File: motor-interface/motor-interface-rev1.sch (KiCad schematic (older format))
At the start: 24 parts

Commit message: Done with 1st pass of interface board schematic
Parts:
- added RV? (x3): POT, symbol POT
- added U? (x2): SN74LV1T34, symbol SN74LV1T34
- R?: value R_Small -> 330R
- R?: value R_Small -> 500R
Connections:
- net +3V3: now also P?.2 (P2), U?.5 (VCC), U?.5 (VCC), U?.5 (VCC)
- net GND: now also RV?.3, RV?.3, RV?.3, U?.3 (GND), U?.3 (GND)
- net at P?.1 (P1), P?.13 (P13): now also U?.2 (A)
- net at P?.7 (P7), Q?.1 (G): now also U?.4 (Y); no longer P?.11 (P11)
- net +5V: now reaches D?.2 (A), P?.18 (P18), U?.1 (VI)
- net +5V: now also U?.5 (VCC), U?.5 (VCC), U?.5 (VCC)
- net at P?.19 (P19): now also RV?.1
- net at P?.21 (P21): now also RV?.1
- net at P?.23 (P23): now also RV?.1
- net at P?.14 (P14), P?.3 (P3): now also U?.4 (Y)
- net at P?.12 (P12), P?.5 (P5): now also U?.2 (A)
- net at P?.5 (P5), Q?.1 (G): now also U?.4 (Y); no longer P?.9 (P9)
- net at P?.14 (P14), R?.2: now also RV?.2
- net at P?.16 (P16), R?.2: now also RV?.2
- net at P?.18 (P18): now also RV?.2
- net at P?.6 (P6): now also U?.2 (A)
- new net: P?.11 (P11), U?.2 (A)
- new net: P?.9 (P9), U?.2 (A)
- no-connect marks 18 -> 17
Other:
- note added: "GND\nSCS - drv\nCS - temp\nX\nX\nSDI\nSDO\nEN-GATE\nDC-CAL\nX"
- note added: "Hall Effect Output Trim"
- note added: "nFAULT"
- note added: "nOCTW"
- note removed: "GND\nSCS\nX\nX\nX\nSDI\nSDO\nEN-GATE\nDC-CAL\nX"
- moved on the sheet: P?

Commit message: Performed annotation, added 2 missing gnds
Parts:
- gave numbers to parts that had none: 29
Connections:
- net GND: now also P2.4 (P4), P3.2 (P2)

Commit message: Added 3.3V conn to launch, added pots&volt.sensing
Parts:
- added P?: CONN_01X03, symbol CONN_01X03
- added P?: CONN_01X04, symbol CONN_01X04
- added RV? (x4): POT, symbol POT
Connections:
- net +3V3: now also P2.1 (P1)
- net GND: now also RV?.3, RV?.3, RV?.3, RV?.3
- net at P2.10 (P10): now also RV?.2
- net at P2.12 (P12): now also RV?.2
- net at P2.14 (P14), R3.2, RV1.2: now also P?.3 (P3)
- net at P2.16 (P16), R4.2, RV2.2: now also P?.2 (P2)
- net at P2.18 (P18), RV3.2: now also P?.1 (P1)
- net at P2.6 (P6): now also RV?.2
- net at P2.8 (P8): now also RV?.2
- new net: P?.1 (P1), RV?.1
- new net: P?.2 (P2), RV?.1
- new net: P?.3 (P3), RV?.1
- new net: P?.4 (P4), RV?.1
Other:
- note added: "+3.3V Regulator"
- note added: "+5V Buck"
- note added: "Hall Effect Debug"
- note added: "Launchpad Left"
- note added: "Launchpad Right"
- note added: "Motor Control Board"
- note added: "VC-FB\nVB-FB\nVA-FB\nDC-V-FB"
- note added: "Voltage Feedback Trim"
- note added: "Voltage Sensing"
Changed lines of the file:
@@
 Wire Wire Line
 	4900 4250 4800 4250
+$Comp
+L +3.3V #PWR?
+U 1 1 56FC658F
+P 2700 4100
+F 0 "#PWR?" H 2700 3950 50  0001 C CNN
+F 1 "+3.3V" H 2700 4240 50  0000 C CNN
+F 2 "" H 2700 4100 50  0000 C CNN
+F 3 "" H 2700 4100 50  0000 C CNN
+	1    2700 4100
+	1    0    0    -1
+$EndComp
+Wire Wire Line
+	2700 4100 2700 4250
+$Comp
+L CONN_01X03 P?
+U 1 1 56FC81E5
+P 3100 7700
+F 0 "P?" H 3100 7900 50  0000 C CNN
+F 1 "CONN_01X03" V 3200 7700 50  0000 C CNN
+F 2 "" H 3100 7700 50  0000 C CNN
+F 3 "" H 3100 7700 50  0000 C CNN
+	1    3100 7700
+	0    1    1    0
+$EndComp
+Text Notes 2750 7950 0    60   ~ 0
+Hall Effect Debug
+Wire Notes Line
+	2850 7850 3350 7850
+Wire Notes Line
+	3350 7850 3350 7450
+Wire Notes Line
+	3350 7450 2850 7450
+Wire Notes Line
+	2850 7450 2850 7850
+Wire Wire Line
+	3000 7500 3000 7300
+Connection ~ 3000 7300
+Wire Wire Line
+	3100 7500 3100 7250
+Connection ~ 3100 7250
+Wire Wire Line
+	3200 7500 3200 6750
+Connection ~ 3200 6750
+$Comp
+L CONN_01X04 P?
+U 1 1 56FC95E7
+P 5350 7100
+F 0 "P?" H 5350 7350 50  0000 C CNN
+F 1 "CONN_01X04" V 5450 7100 50  0000 C CNN
+F 2 "" H 5350 7100 50  0000 C CNN
+F 3 "" H 5350 7100 50  0000 C CNN
+	1    5350 7100
+	1    0    0    -1
+$EndComp
+Wire Wire Line
+	3850 6650 3850 4450
+Wire Wire Line
+	3850 4450 3200 4450
+Wire Wire Line
+	3800 6750 3800 4550
+Wire Wire Line
+	3800 4550 3200 4550
+Wire Wire Line
+	3750 6850 3750 4650
+Wire Wire Line
+	3750 4650 3200 4650
+Wire Wire Line
+	3700 4750 3700 7550
+Wire Wire Line
+	3700 4750 3200 4750
+Wire Notes Line
+	5150 6800 5150 7400
+Wire Notes Line
+	5150 7400 5550 7400
+Wire Notes Line
+	5550 7400 5550 6800
+Wire Notes Line
+	5550 6800 5150 6800
+Text Notes 5050 6750 0    60   ~ 0
+Voltage Sensing
+$Comp
+L POT RV?
+U 1 1 56FC9C0F
+P 4700 7550
+F 0 "RV?" H 4700 7450 50  0000 C CNN
+F 1 "POT" H 4700 7550 50  0000 C CNN
+F 2 "" H 4700 7550 50  0000 C CNN
+F 3 "" H 4700 7550 50  0000 C CNN
+	1    4700 7550
+	0    -1   1    0
+$EndComp
+$Comp
+L POT RV?
+U 1 1 56FC9CC4
+P 5050 7550
+F 0 "RV?" H 5050 7450 50  0000 C CNN
+F 1 "POT" H 5050 7550 50  0000 C CNN
+F 2 "" H 5050 7550 50  0000 C CNN
+F 3 "" H 5050 7550 50  0000 C CNN
+	1    5050 7550
+	0    -1   1    0
+$EndComp
+$Comp
+L POT RV?
+U 1 1 56FC9D25
+P 4000 7550
+F 0 "RV?" H 4000 7450 50  0000 C CNN
+F 1 "POT" H 4000 7550 50  0000 C CNN
+F 2 "" H 4000 7550 50  0000 C CNN
+F 3 "" H 4000 7550 50  0000 C CNN
+	1    4000 7550
+	0    -1   1    0
+$EndComp
+$Comp
+L POT RV?
+U 1 1 56FC9D8A
+P 4350 7550
+F 0 "RV?" H 4350 7450 50  0000 C CNN
+F 1 "POT" H 4350 7550 50  0000 C CNN
+F 2 "" H 4350 7550 50  0000 C CNN
+F 3 "" H 4350 7550 50  0000 C CNN
+	1    4350 7550
+	0    -1   1    0
+$EndComp
+$Comp
+L GND #PWR?
+U 1 1 56FCA3E0
+P 4000 7850
+F 0 "#PWR?" H 4000 7600 50  0001 C CNN
+F 1 "GND" H 4000 7700 50  0000 C CNN
+F 2 "" H 4000 7850 50  0000 C CNN
+F 3 "" H 4000 7850 50  0000 C CNN
+	1    4000 7850
+	1    0    0    -1
+$EndComp
+$Comp
+L GND #PWR?
+U 1 1 56FCA45B
+P 4350 7850
+F 0 "#PWR?" H 4350 7600 50  0001 C CNN
+F 1 "GND" H 4350 7700 50  0000 C CNN
+F 2 "" H 4350 7850 50  0000 C CNN
+F 3 "" H 4350 7850 50  0000 C CNN
+	1    4350 7850
+	1    0    0    -1
+$EndComp
+$Comp
+L GND #PWR?
+U 1 1 56FCA4CF
+P 4700 7850
+F 0 "#PWR?" H 4700 7600 50  0001 C CNN
+F 1 "GND" H 4700 7700 50  0000 C CNN
+F 2 "" H 4700 7850 50  0000 C CNN
+F 3 "" H 4700 7850 50  0000 C CNN
+	1    4700 7850
+	1    0    0    -1
+$EndComp
+$Comp
+L GND #PWR?
+U 1 1 56FCA543
+P 5050 7850
+F 0 "#PWR?" H 5050 7600 50  0001 C CNN
+F 1 "GND" H 5050 7700 50  0000 C CNN
+F 2 "" H 5050 7850 50  0000 C CNN
+F 3 "" H 5050 7850 50  0000 C CNN
+	1    5050 7850
+	1    0    0    -1
+$EndComp
+Wire Wire Line
+	4000 7800 4000 7850
+Wire Wire Line
+	4350 7800 4350 7850
+Wire Wire Line
+	4700 7800 4700 7850
+Wire Wire Line
+	5050 7800 5050 7850
+Wire Wire Line
+	5050 7300 5050 7250
+Wire Wire Line
+	5050 7250 5150 7250
+Wire Wire Line
+	4700 7300 4700 7150
+Wire Wire Line
+	4700 7150 5150 7150
+Wire Wire Line
+	4350 7300 4350 7050
+Wire Wire Line
+	4350 7050 5150 7050
+Wire Wire Line
+	4000 7300 4000 6950
+Wire Wire Line
+	4000 6950 5150 6950
+Wire Wire Line
+	3700 7550 3850 7550
+Wire Wire Line
+	4200 7550 4200 6850
+Wire Wire Line
+	4200 6850 3750 6850
+Wire Wire Line
+	4550 7550 4550 6750
+Wire Wire Line
+	4550 6750 3800 6750
+Wire Wire Line
+	4900 7550 4900 6650
+Wire Wire Line
+	4900 6650 3850 6650
+Text Notes 5550 7250 0    60   ~ 0
+VC-FB\nVB-FB\nVA-FB\nDC-V-FB
+Wire Notes Line
+	3850 7300 5150 7300
+Wire Notes Line
+	5150 7300 5150 7800
+Wire Notes Line
+	5150 7800 3850 7800
+Wire Notes Line
+	3850 7800 3850 7300
+Text Notes 5150 7750 0    60   ~ 0
+Voltage Feedback Trim
+Text Notes 6000 1100 0    60   ~ 0
++5V Buck
+Text Notes 7100 1300 0    60   ~ 0
++3.3V Regulator
+Text Notes 2750 4100 0    60   ~ 0
+Launchpad Left
+Text Notes 4250 4100 0    60   ~ 0
+Launchpad Right
+Text Notes 2400 1850 0    60   ~ 0
+Motor Control Board
 $EndSCHEMATC

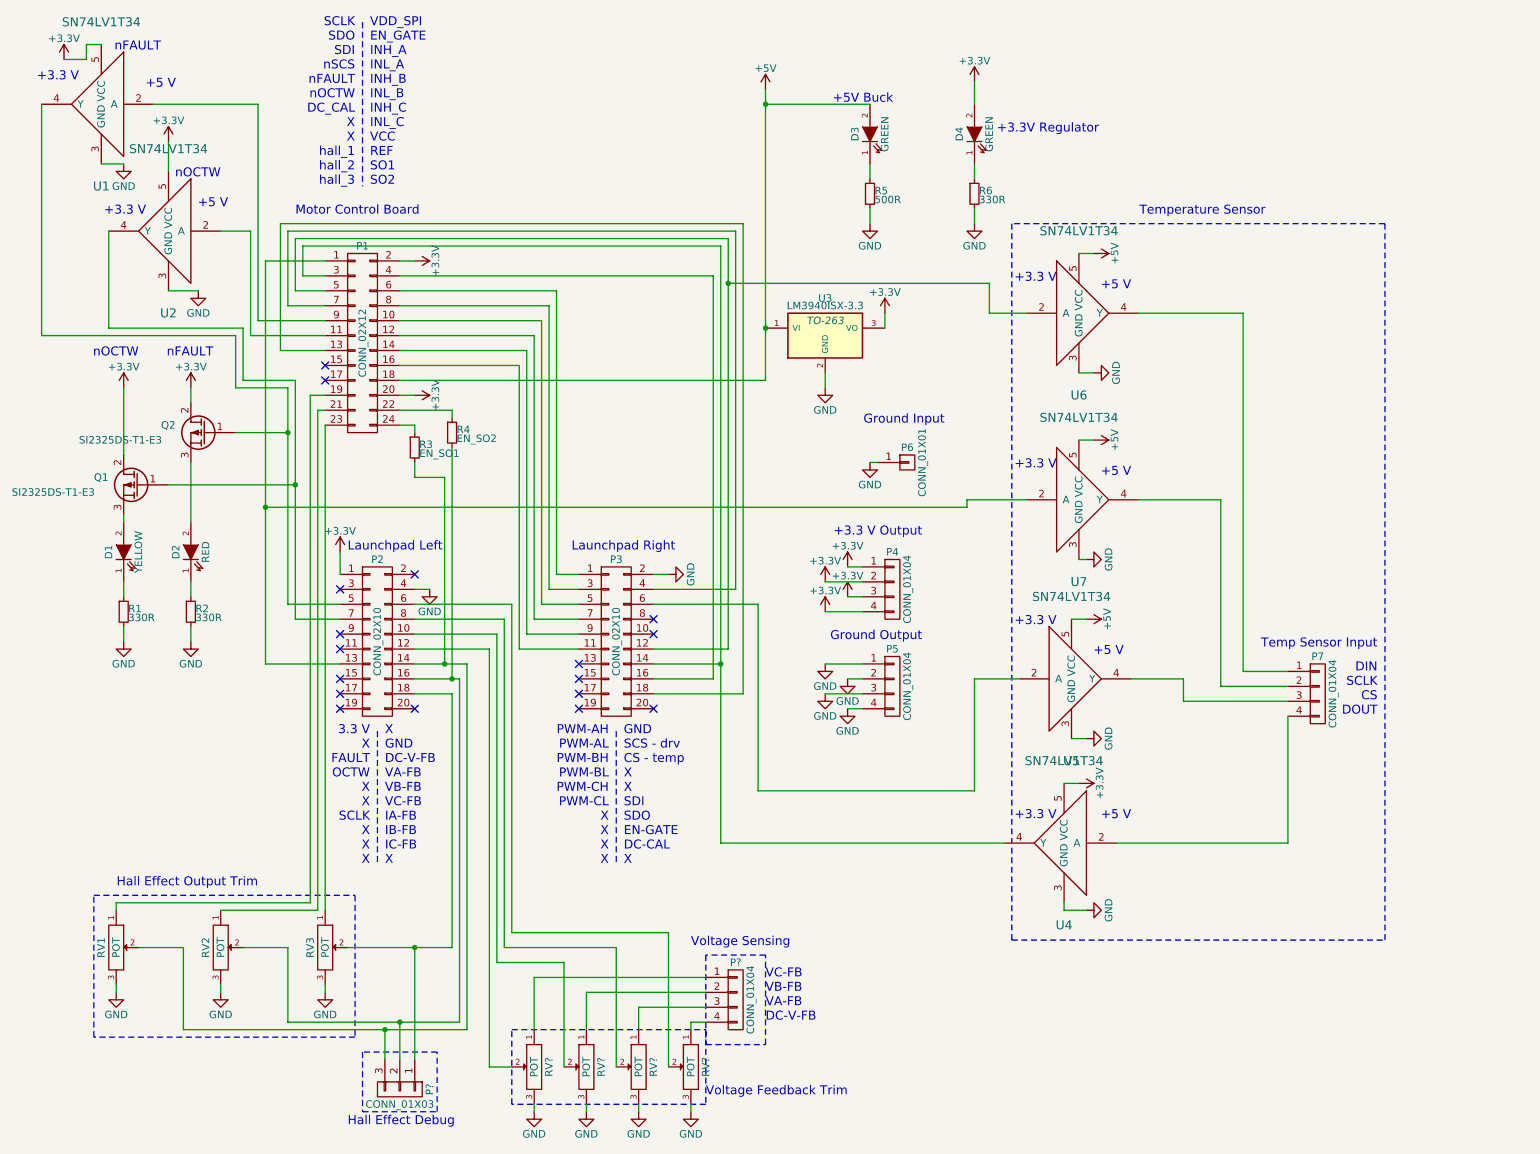
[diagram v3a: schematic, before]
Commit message: newftprnts,ftprntassoc.bckup3.3to5v,etc
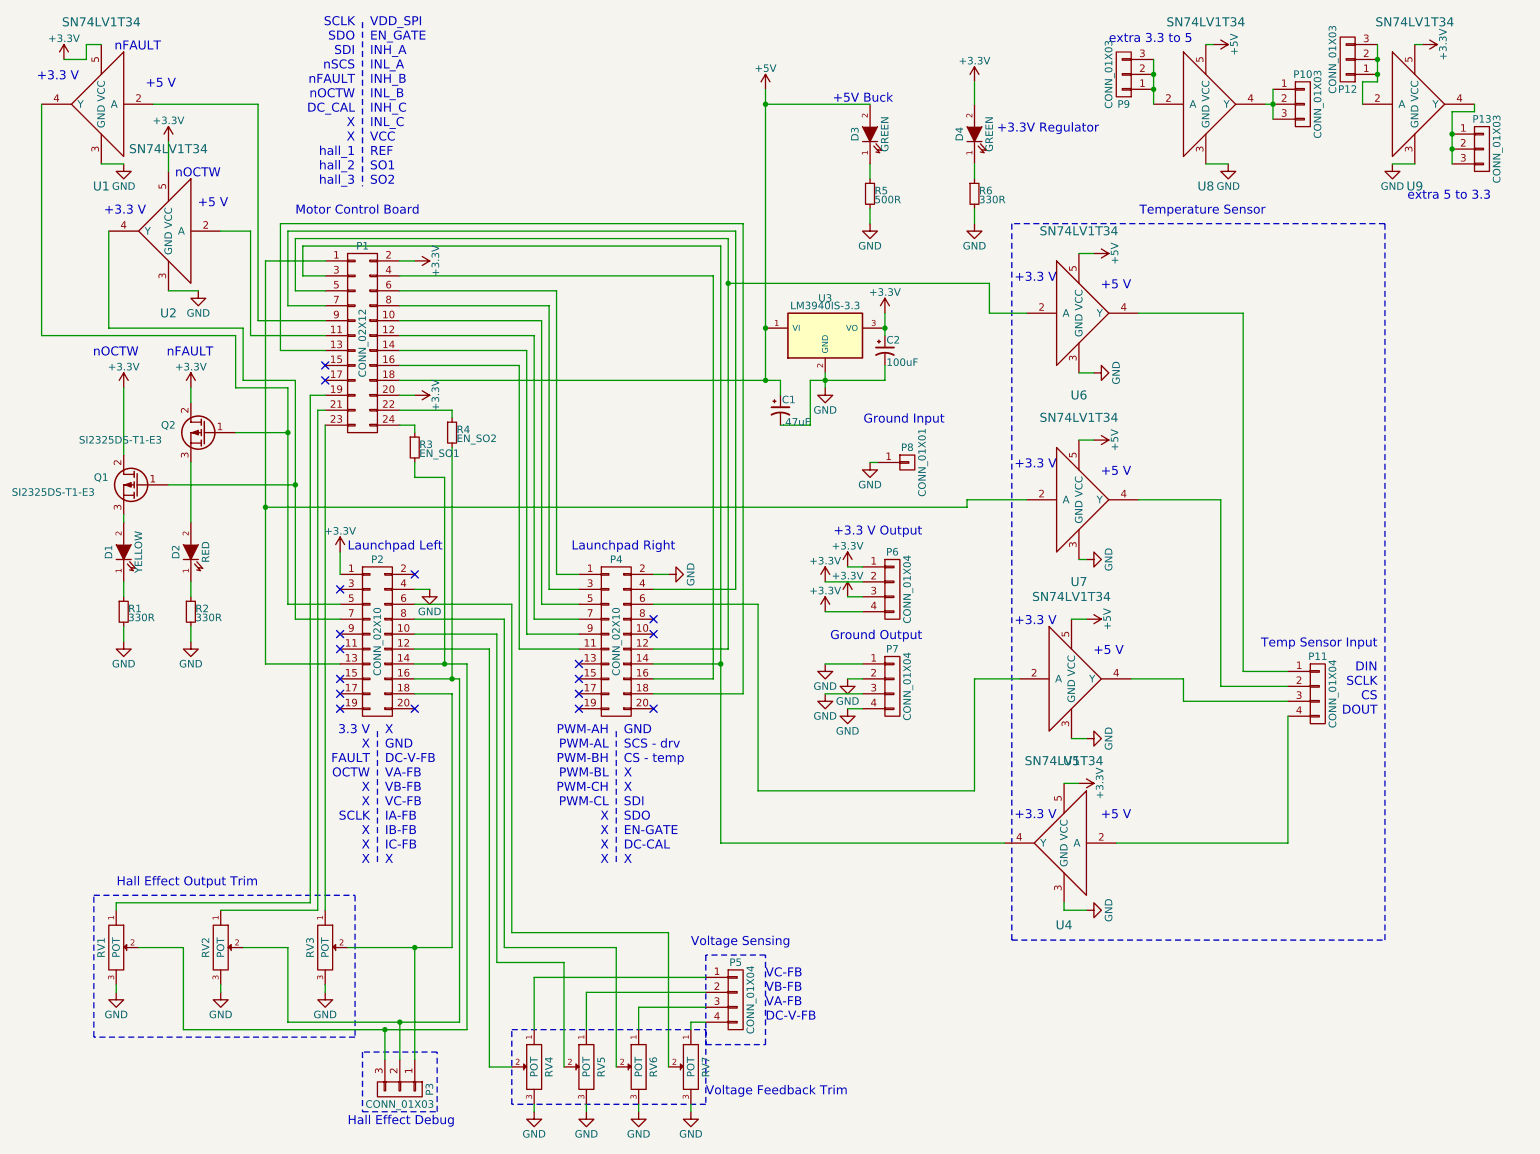
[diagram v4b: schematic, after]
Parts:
- added C1: .47uF, Capacitors_Tantalum_SMD:TantalC_SizeB_EIA-3528_Reflow, symbol CP1_Small
- added C2: 100uF, Capacitors_Tantalum_SMD:TantalC_SizeA_EIA-3216_Reflow, symbol CP1_Small
- added P10, P12, P13, P9: CONN_01X03, Pin_Headers:Pin_Header_Straight_1x03, symbol CONN_01X03
- added U8, U9: SN74LV1T34, p16261:SN74LV1T34, symbol SN74LV1T34
- D1, D2, D3, D4: footprint (none) -> LEDs:LED-0805
- P1: footprint (none) -> Pin_Headers:Pin_Header_Straight_2x12
- P11: renamed from P7; footprint (none) -> Pin_Headers:Pin_Header_Straight_1x04
- P2: footprint (none) -> Pin_Headers:Pin_Header_Straight_2x10
- P3: renamed from P?; footprint (none) -> Pin_Headers:Pin_Header_Straight_1x03
- P4: renamed from P3; footprint (none) -> Pin_Headers:Pin_Header_Straight_2x10
- P5: renamed from P?; footprint (none) -> Pin_Headers:Pin_Header_Straight_1x04
- P6: renamed from P4; footprint (none) -> Pin_Headers:Pin_Header_Straight_1x04
- P7: renamed from P5; footprint (none) -> Pin_Headers:Pin_Header_Straight_1x04
- P8: renamed from P6; footprint (none) -> Pin_Headers:Pin_Header_Straight_1x01
- Q1, Q2: footprint (none) -> p16261:SI2325DS-T1-E3
- R1, R2, R3, R4, R5, R6: footprint (none) -> Resistors_SMD:R_0805
- RV1, RV2, RV3: footprint (none) -> p16261:3361P
- RV4, RV5, RV6, RV7: renamed from RV?; footprint (none) -> p16261:3361P
- U1, U2, U4, U5, U6, U7: footprint (none) -> p16261:SN74LV1T34
- U3: value LM3940ISX-3.3 -> LM3940IS-3.3; footprint TO-263 -> p16261:LM3940IS-3.3
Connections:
- net +3V3: now also C2.1, U9.5 (VCC)
- net +5V: now also C1.1, U8.5 (VCC)
- net GND: now also C1.2, C2.2, U8.3 (GND), U9.3 (GND)
- new net: P9.1 (P1), P9.2 (P2), P9.3 (P3), U8.2 (A)
- new net: P10.1 (P1), P10.2 (P2), P10.3 (P3), U8.4 (Y)
- new net: P12.1 (P1), P12.2 (P2), P12.3 (P3), U9.2 (A)
- new net: P13.1 (P1), P13.2 (P2), P13.3 (P3), U9.4 (Y)
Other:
- note added: "extra 3.3 to 5"
- note added: "extra 5 to 3.3"

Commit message: Added keepouts, progress on layout
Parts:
- R1, R2, R3, R4, R5, R6: footprint Resistors_SMD:R_0805 -> Resistors_SMD:R_0603
- RV1, RV2, RV3, RV4, RV5, RV6, RV7: symbol POT -> POT-RESCUE-motor-interface-rev1
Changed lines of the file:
@@
 EESchema Schematic File Version 2
+LIBS:motor-interface-rev1-rescue
 LIBS:power
 LIBS:device
@@
 F 0 "R3" H 3230 3420 50  0000 L CNN
 F 1 "EN_SO1" H 3230 3360 50  0000 L CNN
-F 2 "Resistors_SMD:R_0805" H 3200 3400 50  0001 C CNN
+F 2 "Resistors_SMD:R_0603" H 3200 3400 50  0001 C CNN
 F 3 "" H 3200 3400 50  0000 C CNN
 	1    3200 3400
@@
 F 0 "R4" H 3480 3320 50  0000 L CNN
 F 1 "EN_SO2" H 3480 3260 50  0000 L CNN
-F 2 "Resistors_SMD:R_0805" H 3450 3300 50  0001 C CNN
+F 2 "Resistors_SMD:R_0603" H 3450 3300 50  0001 C CNN
 F 3 "" H 3450 3300 50  0000 C CNN
 	1    3450 3300
@@
 F 0 "R1" H 1280 4520 50  0000 L CNN
 F 1 "330R" H 1280 4460 50  0000 L CNN
-F 2 "Resistors_SMD:R_0805" H 1250 4500 50  0001 C CNN
+F 2 "Resistors_SMD:R_0603" H 1250 4500 50  0001 C CNN
 F 3 "" H 1250 4500 50  0000 C CNN
 	1    1250 4500
@@
 F 0 "R2" H 1730 4520 50  0000 L CNN
 F 1 "330R" H 1730 4460 50  0000 L CNN
-F 2 "Resistors_SMD:R_0805" H 1700 4500 50  0001 C CNN
+F 2 "Resistors_SMD:R_0603" H 1700 4500 50  0001 C CNN
 F 3 "" H 1700 4500 50  0000 C CNN
 	1    1700 4500
@@
 F 0 "R6" H 6980 1720 50  0000 L CNN
 F 1 "330R" H 6980 1660 50  0000 L CNN
-F 2 "Resistors_SMD:R_0805" H 6950 1700 50  0001 C CNN
+F 2 "Resistors_SMD:R_0603" H 6950 1700 50  0001 C CNN
 F 3 "" H 6950 1700 50  0000 C CNN
 	1    6950 1700
@@
 F 0 "R5" H 6280 1720 50  0000 L CNN
 F 1 "500R" H 6280 1660 50  0000 L CNN
-F 2 "Resistors_SMD:R_0805" H 6250 1700 50  0001 C CNN
+F 2 "Resistors_SMD:R_0603" H 6250 1700 50  0001 C CNN
 F 3 "" H 6250 1700 50  0000 C CNN
 	1    6250 1700
@@
 +5 V
 $Comp
-L POT RV1
+L POT-RESCUE-motor-interface-rev1 RV1
 U 1 1 56F10C2C
 P 1200 6750
@@
 $EndComp
 $Comp
-L POT RV2
+L POT-RESCUE-motor-interface-rev1 RV2
 U 1 1 56F110C8
 P 1900 6750
@@
 $EndComp
 $Comp
-L POT RV3
+L POT-RESCUE-motor-interface-rev1 RV3
 U 1 1 56F11138
 P 2600 6750
@@
 Voltage Sensing
 $Comp
-L POT RV6
+L POT-RESCUE-motor-interface-rev1 RV6
 U 1 1 56FC9C0F
 P 4700 7550
@@
 $EndComp
 $Comp
-L POT RV7
+L POT-RESCUE-motor-interface-rev1 RV7
 U 1 1 56FC9CC4
 P 5050 7550
@@
 $EndComp
 $Comp
-L POT RV4
+L POT-RESCUE-motor-interface-rev1 RV4
 U 1 1 56FC9D25
 P 4000 7550
@@
 $EndComp
 $Comp
-L POT RV5
+L POT-RESCUE-motor-interface-rev1 RV5
 U 1 1 56FC9D8A
 P 4350 7550
